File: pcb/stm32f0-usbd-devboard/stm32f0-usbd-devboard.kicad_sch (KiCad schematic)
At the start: 23 parts, among them J1 USB_B_Mini, J2 PIN H 5P, J3 LEFT, J4 RIGHT, U1 USBLC6-2SC6, U2 MCP1700-3302E, U3 STM32F042K4T6 or STM32F042K6T6

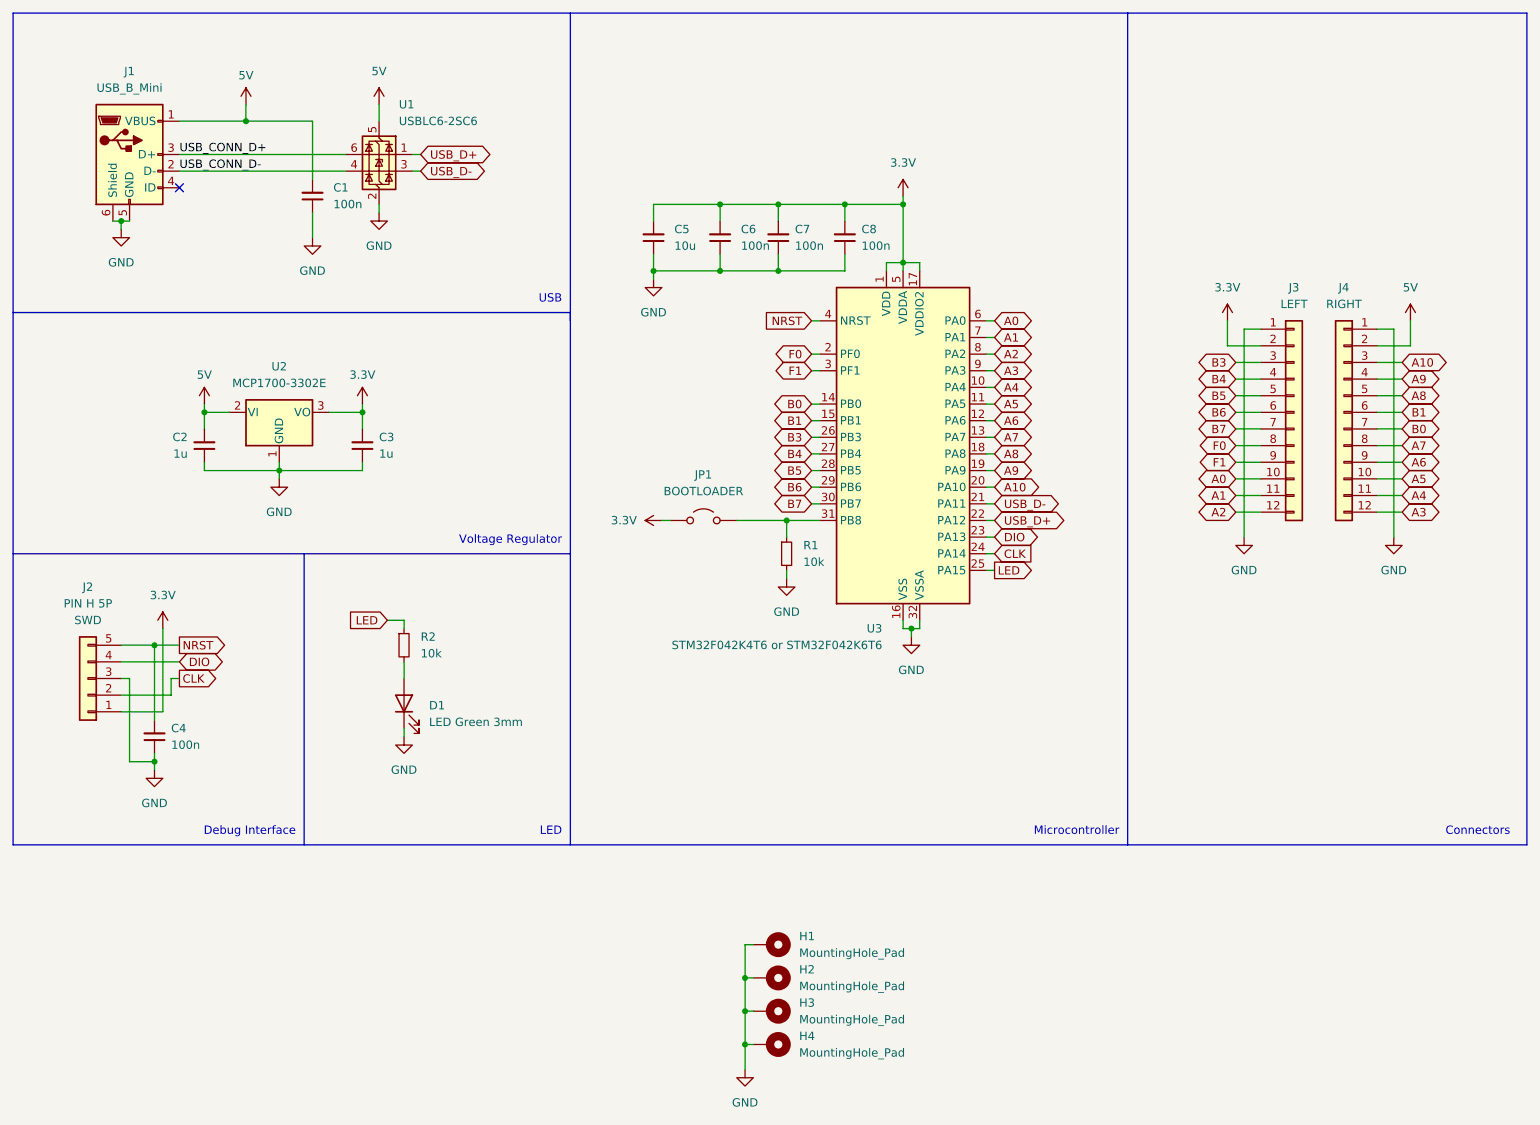
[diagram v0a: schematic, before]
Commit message: pcb: *: new revision: 20250412
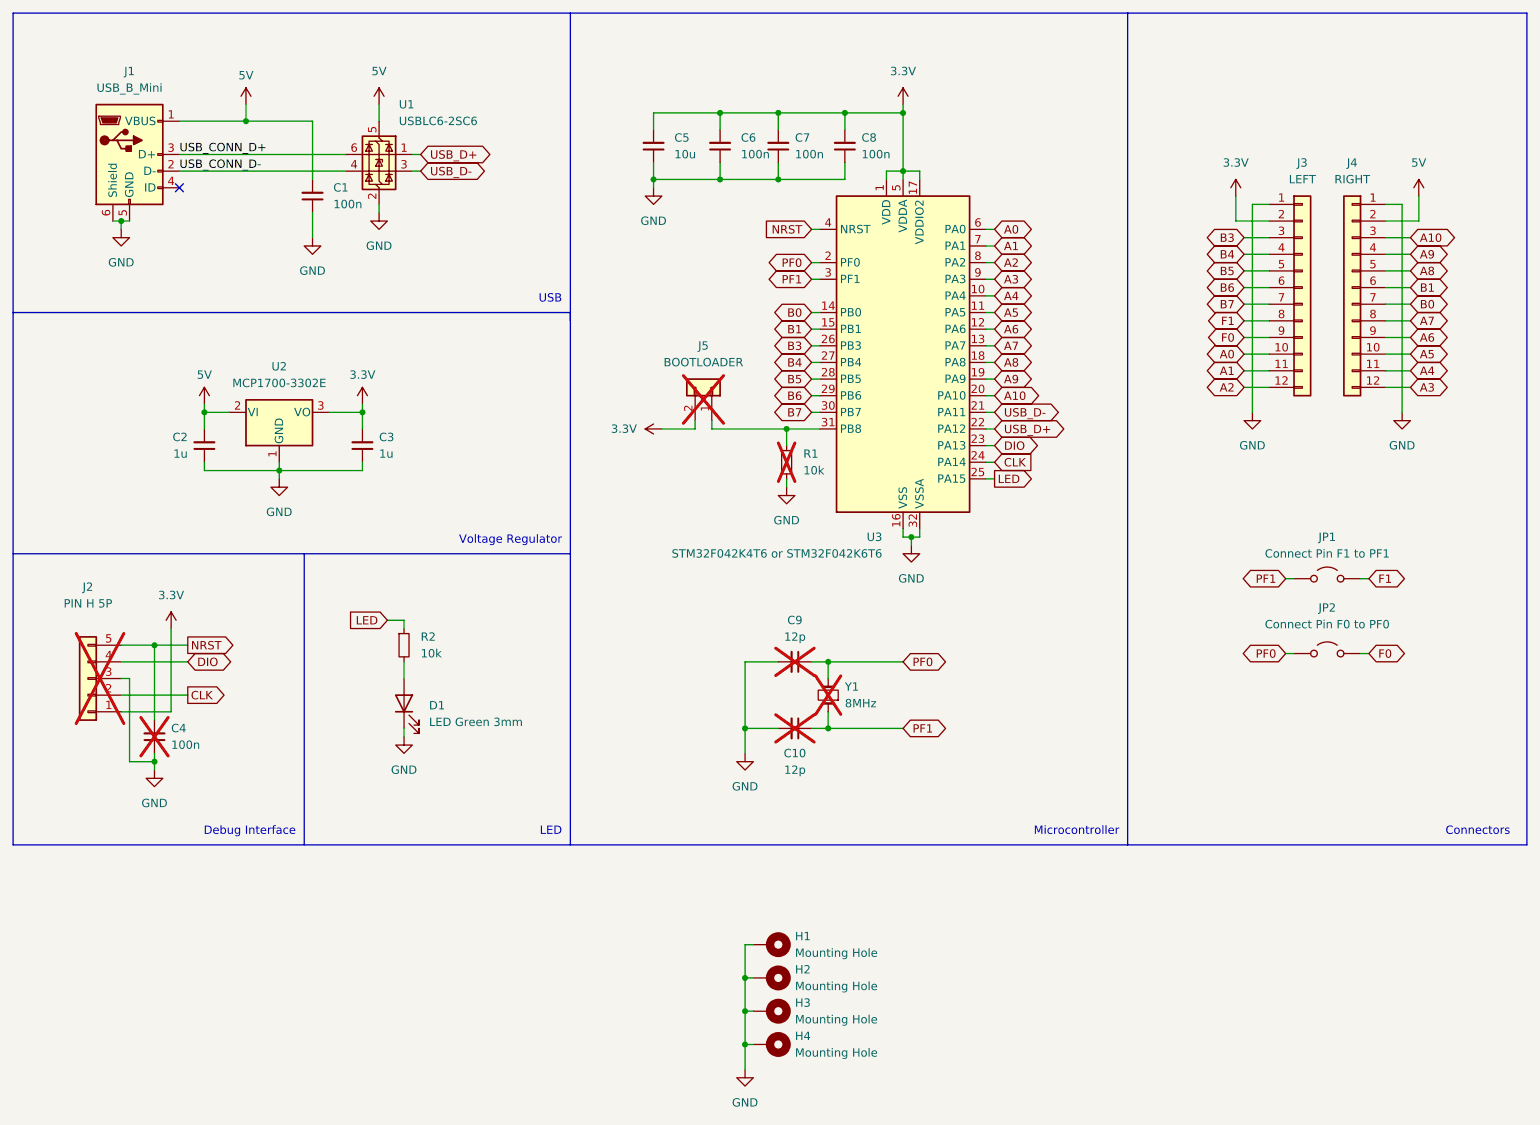
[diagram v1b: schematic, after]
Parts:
- added C10, C9: 12p, Capacitor_THT:C_Disc_D3.8mm_W2.6mm_P2.50mm, symbol Device:C_Small
- added JP1: Connect Pin F1 to PF1, Jumper:SolderJumper-2_P1.3mm_Open_TrianglePad1.0x1.5mm, symbol Jumper:Jumper_2_Open
- added JP2: Connect Pin F0 to PF0, Jumper:SolderJumper-2_P1.3mm_Open_TrianglePad1.0x1.5mm, symbol Jumper:Jumper_2_Open
- added Y1: 8MHz, Crystal:Crystal_HC49-4H_Vertical, symbol Device:Crystal_Small
- C4, R1: now not fitted
- H1, H2, H3, H4: value MountingHole_Pad -> Mounting Hole
- J2: Descr SWD -> (none); STM32_PIN2 (none) -> A14; STM32_PIN4 (none) -> A13; now not fitted
- J5: renamed from JP1; footprint Connector_PinHeader_2.54mm:PinHeader_1x02_P2.54mm_Vertical -> custom:PinHeader_Bootloader_1x02_P2.54mm_Horizontal; symbol Jumper:Jumper_2_Open -> Connector_Generic:Conn_01x02; now not fitted
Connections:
- net F0: now also J3.9 (Pin_9), JP2.1 (A); no longer J3.8 (Pin_8), U3.2 (PF0)
- net F1: now also J3.8 (Pin_8), JP1.1 (A); no longer J3.9 (Pin_9), U3.3 (PF1)
- net GND: now also C10.2, C9.2
- new net PF0: C9.1, JP2.2 (B), U3.2 (PF0), Y1.2
- new net PF1: C10.1, JP1.2 (B), U3.3 (PF1), Y1.1
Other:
- moved on the sheet: C5, C6, C7, C8, J3, J4, U3

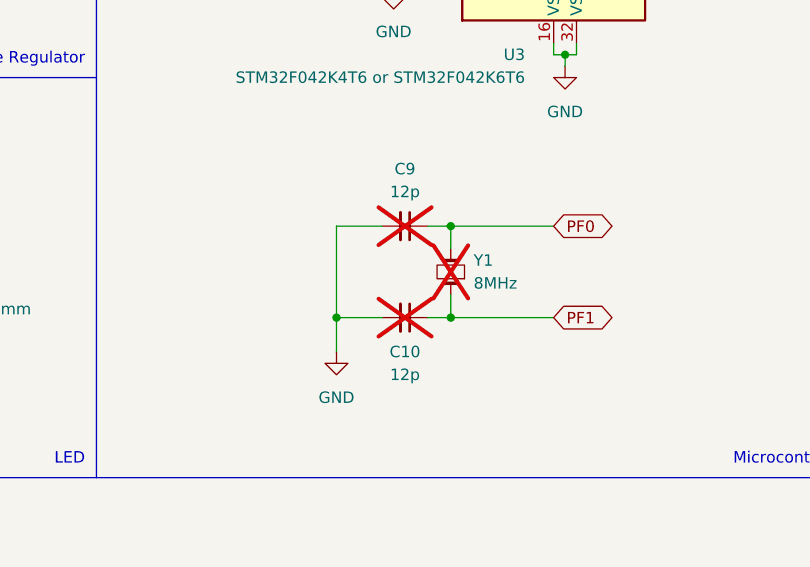
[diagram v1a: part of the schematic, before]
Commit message: pcb: f0: fix crystal capacitor values
trivial fix not affecting any physical layers, not bumping revision.
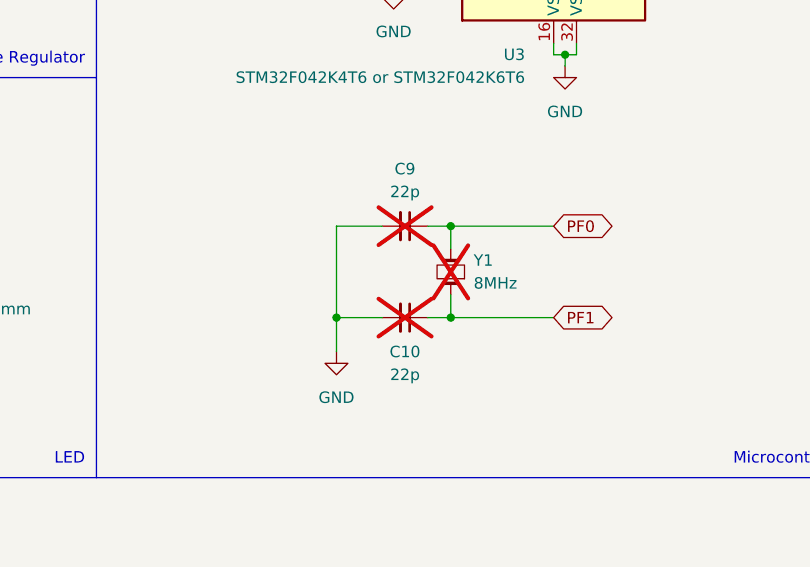
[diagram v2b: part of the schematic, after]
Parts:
- C10, C9: value 12p -> 22p
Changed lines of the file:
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@@
 			)
 		)
-		(property "Value" "12p"
+		(property "Value" "22p"
 			(at 153.6636 143.51 90)
 			(effects
@@
 			)
 		)
-		(property "Value" "12p"
+		(property "Value" "22p"
 			(at 153.6636 123.19 90)
 			(effects
